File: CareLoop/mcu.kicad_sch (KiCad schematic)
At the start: 19 parts, among them J1_DEBUG1 Conn_01x04_Pin, SW1 SW_Push, U6 nRF52840, Y1 32Mhz

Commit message: updated version
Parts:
- removed AE1: Antenna_Chip, RF_Antenna:Johanson_2450AT18x100, symbol Device:Antenna_Chip
- removed C5: C, symbol Device:C_Small
- added C12: 4.7uF, Capacitor_SMD:C_0603_1608Metric_Pad1.08x0.95mm_HandSolder, symbol Device:C_Small
- added C18: 1.2pF, Capacitor_SMD:C_0603_1608Metric_Pad1.08x0.95mm_HandSolder, symbol Device:C_Small
- added C19: 1pF, Capacitor_SMD:C_0603_1608Metric_Pad1.08x0.95mm_HandSolder, symbol Device:C_Small
- added C27, C28: 14p, Capacitor_SMD:C_0603_1608Metric_Pad1.08x0.95mm_HandSolder, symbol Device:C_Small
- added C5: 1uF, Capacitor_SMD:C_0603_1608Metric_Pad1.08x0.95mm_HandSolder, symbol Device:C
- added L1: 2.2nH, Inductor_SMD:L_0603_1608Metric, symbol Device:L_Small
- added L2: 4.7nH, Inductor_SMD:L_0603_1608Metric, symbol Device:L_Small
- added Y2: 32.768kHz, Crystal:Crystal_SMD_0603-2Pin_6.0x3.5mm, symbol Device:Crystal
- C16: value C -> 820pF; footprint (none) -> Capacitor_SMD:C_0603_1608Metric_Pad1.08x0.95mm_HandSolder
- C17, C7: value C -> 1uF; footprint (none) -> Capacitor_SMD:C_0603_1608Metric_Pad1.08x0.95mm_HandSolder
- C4: value C -> 100nF; footprint (none) -> Capacitor_SMD:C_0603_1608Metric_Pad1.08x0.95mm_HandSolder
- C6: value C -> 100pF; footprint (none) -> Capacitor_SMD:C_0603_1608Metric_Pad1.08x0.95mm_HandSolder
- Y1: value 32Mhz -> 32MHz
- renumbered SW1 to Reset_SW1
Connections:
- net GND: now also D3.1 (K), C12.2, C27.2, C28.2, C5.2
- net at C10.1, U6.A22 (VDD), U6.AD14 (VDD)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: now also C5.1
- net at U6.AC5 (DECUSB): now also C12.1
- net Dminus: now reaches U6.AD4 (D-)
- net Dplus: now reaches U6.AD6 (D+)
- net INT_MAX: now reaches U6.AD8 (P0.13)
- net at U6.D2 (XL1/P0.00): now also C27.1, Y2.2
- net at U6.F2 (XL2/P0.01): now also C28.1, Y2.1
- net VSS_PA: now reaches U6.F23 (VSS_PA)
- net VSS_PA: now also C18.2, C19.2
- net at U6.H23 (ANT): now also C19.1, L2.2
- new net: C18.1, L1.2, L2.1
- new net ANT: L1.1
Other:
- moved on the sheet: C10, C8, C9, D3, J1_DEBUG1, R3, R4, R5, R7, Reset_SW1, U6, Y1

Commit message: WP: update Schematics
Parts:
- added C29: 4.7u, symbol Device:C_Small
- added L5: 10u, symbol Device:L_Small
- added L6: 15n, symbol Device:L_Small
- C17: value 1uF -> 1u; footprint Capacitor_SMD:C_0603_1608Metric_Pad1.08x0.95mm_HandSolder -> (none)
- C18: value 1.2pF -> 1.2p
- C19: value 1pF -> 1p
- C27, C28: value 14p -> 12p
- C5: value 1uF -> 4.7u
- C7: value 1uF -> 47n; footprint Capacitor_SMD:C_0603_1608Metric_Pad1.08x0.95mm_HandSolder -> (none)
- L1: value 2.2nH -> 2.2n
- L2: value 4.7nH -> 4.7n
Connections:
- net VSS_PA is gone; now on net GND: C18.2, C19.2, U6.F23 (VSS_PA)
- net GND: now also C17.2, C7.2, C29.2; no longer C17.1, C7.1
- net VCC: now also C10.1, C5.1, U6.A22 (VDD), U6.AD14 (VDD), U6.AD23 (VDD), U6.B1 (VDD), U6.W1 (VDD), U6.Y2 (VDDH)
- net at U6.E24 (DEC6): now also C17.1, C7.1, U6.B5 (DEC4), L6.2; no longer C17.2
- net VBUS: now reaches U6.AD2 (VBUS)
- net VBUS: now also C29.1
- net at U6.B3 (DCC): now also L5.1
- new net: L5.2, L6.1

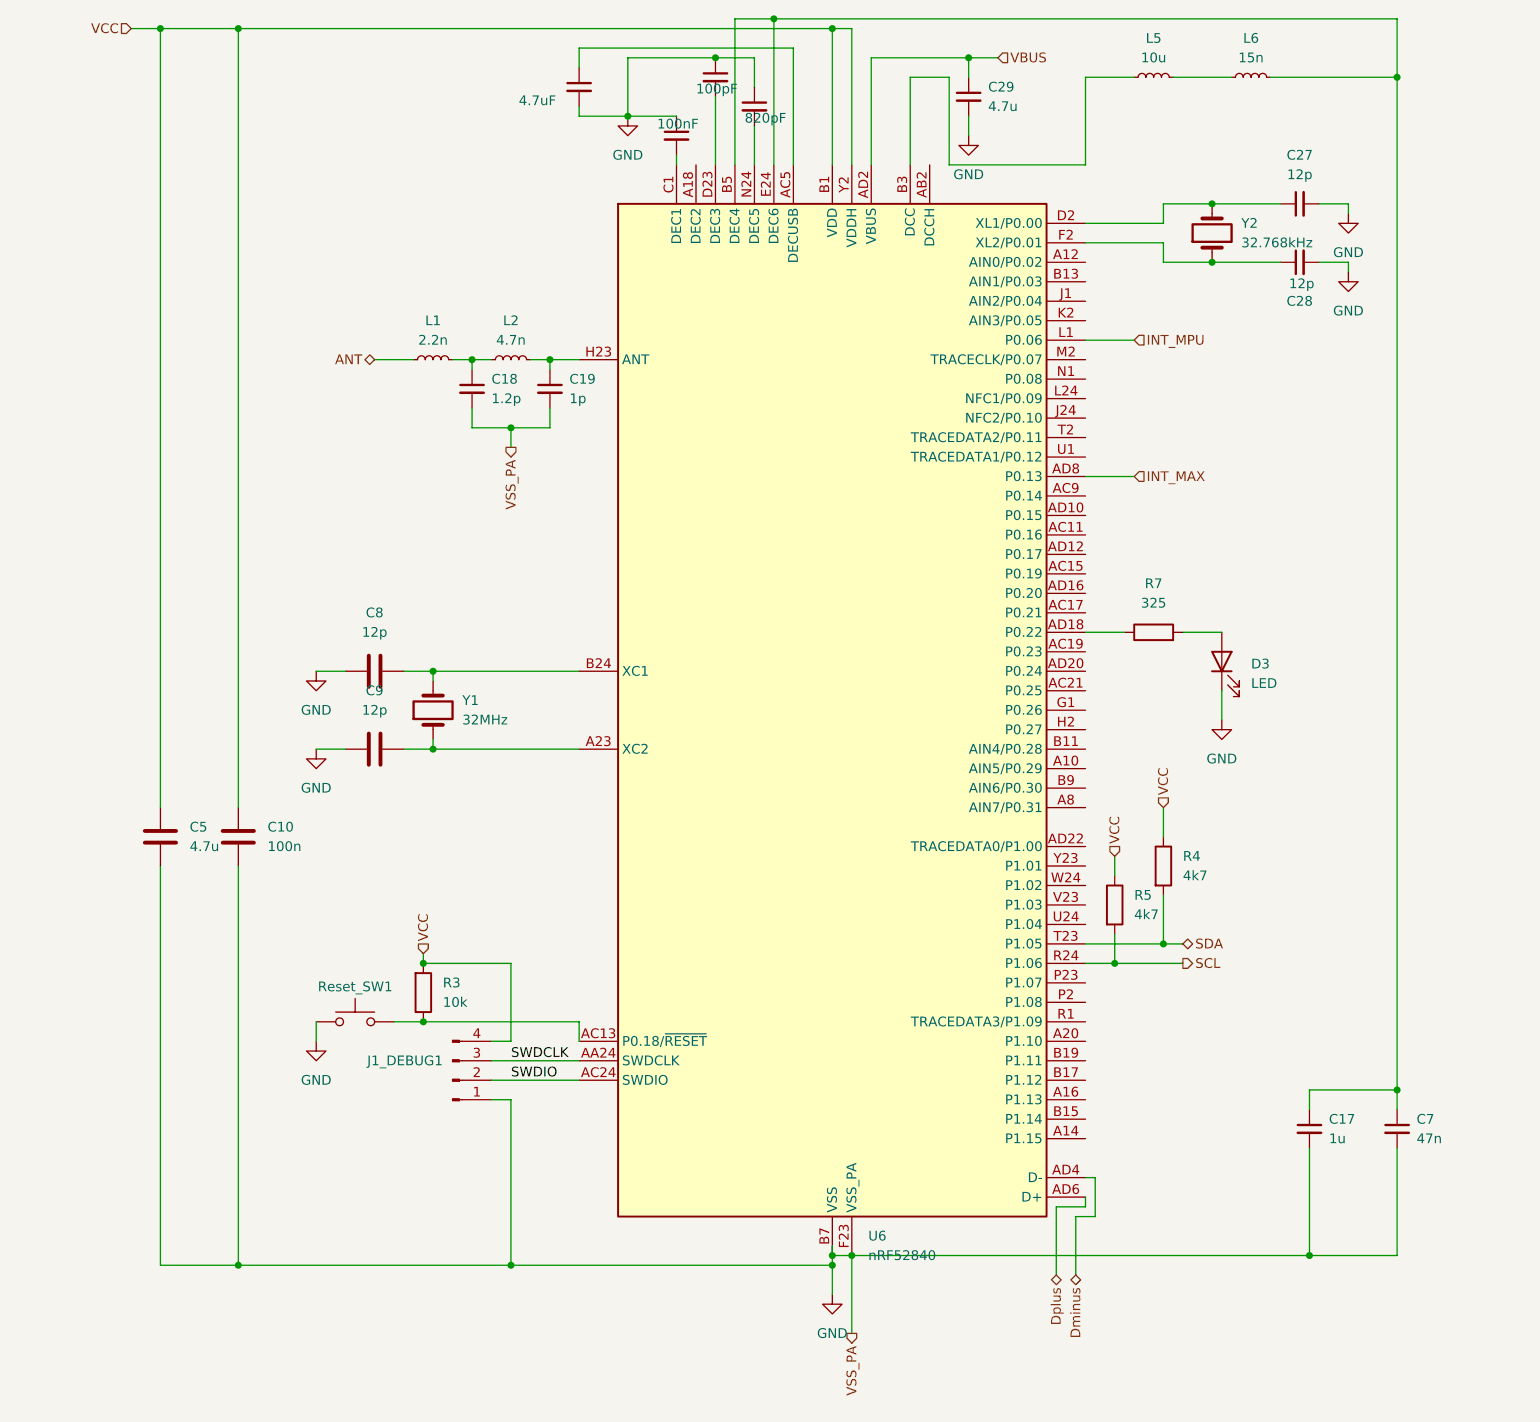
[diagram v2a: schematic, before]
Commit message: WP: Placement PCB Parts done
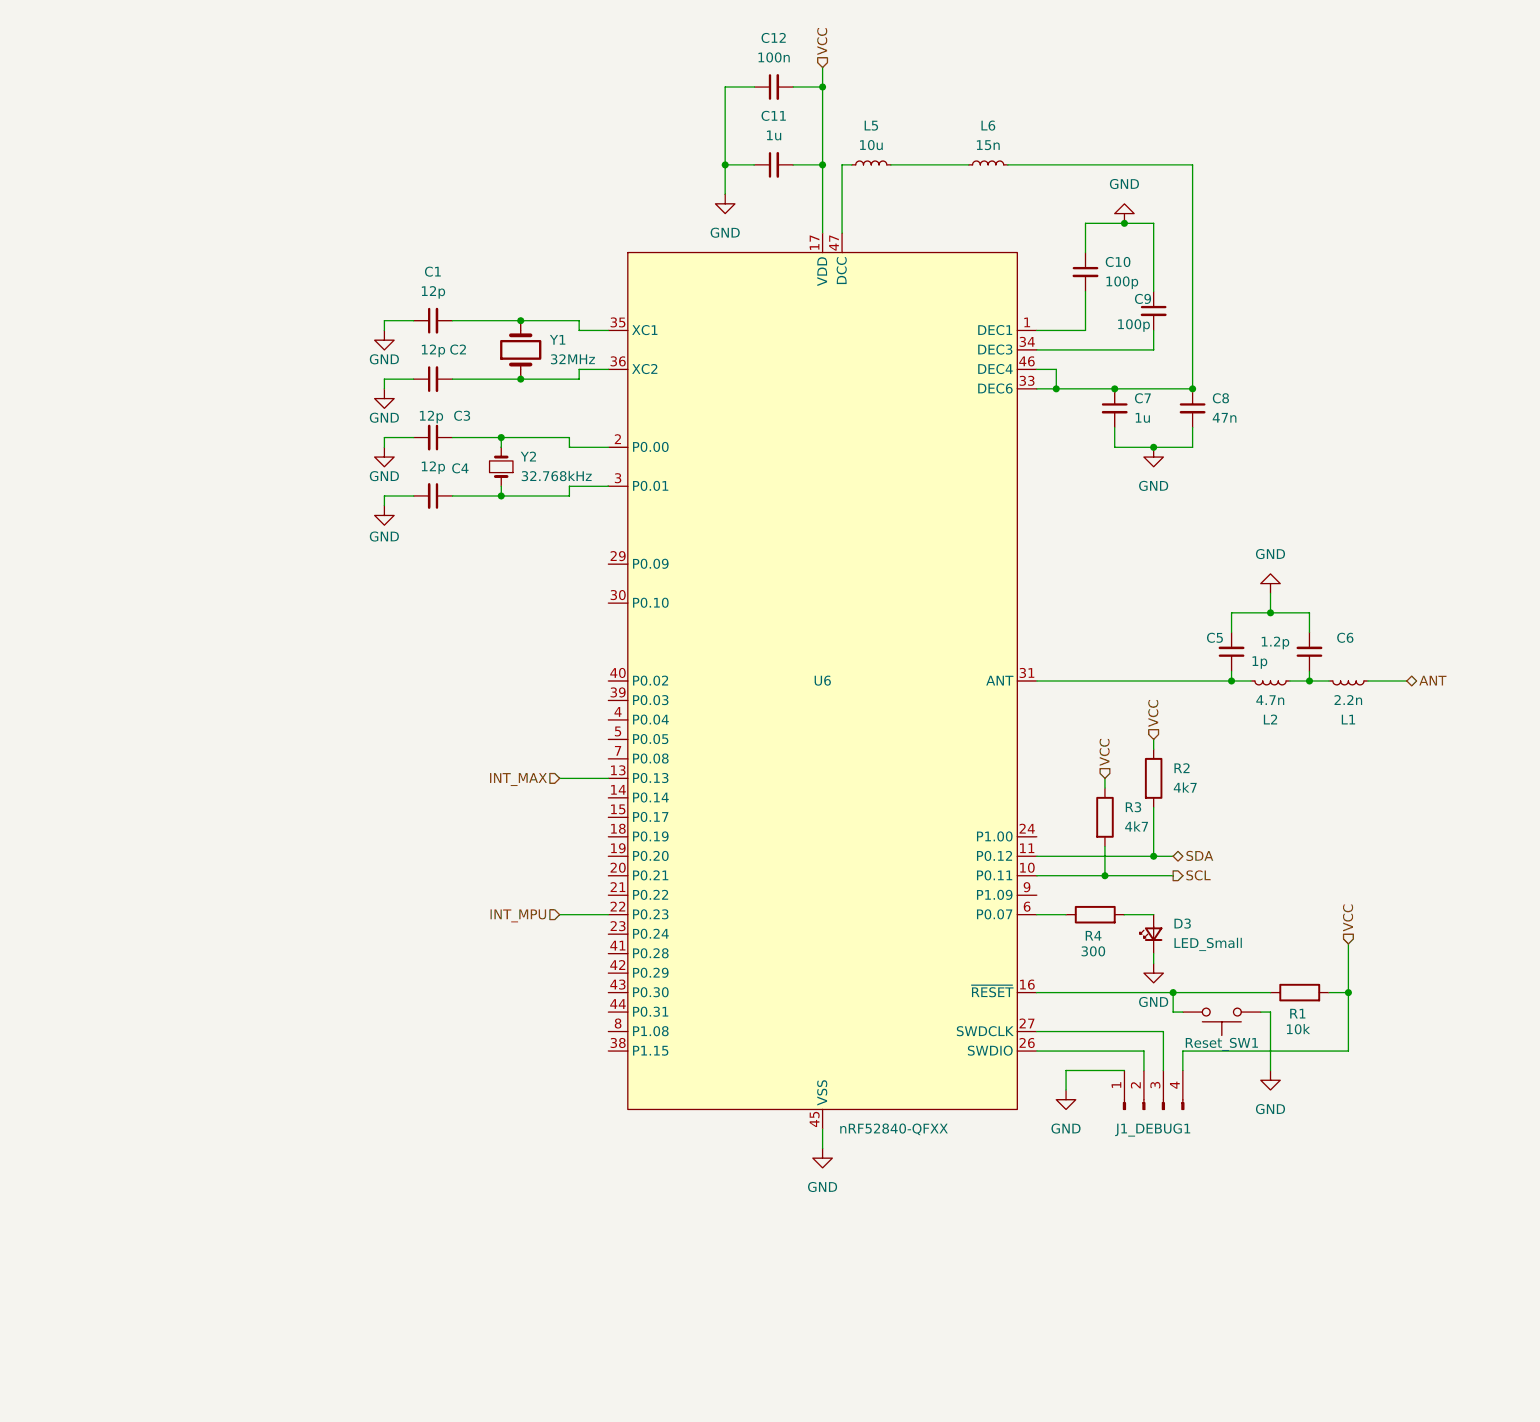
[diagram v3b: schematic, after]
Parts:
- removed C10: 100n, Capacitor_SMD:C_0603_1608Metric_Pad1.08x0.95mm_HandSolder, symbol Device:C
- removed C16: 820pF, Capacitor_SMD:C_0603_1608Metric_Pad1.08x0.95mm_HandSolder, symbol Device:C_Small
- removed C17: 1u, symbol Device:C_Small
- removed C29: 4.7u, symbol Device:C_Small
- removed C4: 100nF, Capacitor_SMD:C_0603_1608Metric_Pad1.08x0.95mm_HandSolder, symbol Device:C_Small
- removed C5: 4.7u, Capacitor_SMD:C_0603_1608Metric_Pad1.08x0.95mm_HandSolder, symbol Device:C
- removed C6: 100pF, Capacitor_SMD:C_0603_1608Metric_Pad1.08x0.95mm_HandSolder, symbol Device:C_Small
- removed C8, C9: 12p, Capacitor_SMD:C_0603_1608Metric_Pad1.08x0.95mm_HandSolder, symbol Device:C
- removed D3: LED, LED_SMD:LED_1206_3216Metric_Pad1.42x1.75mm_HandSolder, symbol Device:LED
- removed R3: 10k, Resistor_SMD:R_0603_1608Metric_Pad0.98x0.95mm_HandSolder, symbol Device:R
- removed U6: nRF52840, Package_DFN_QFN:Nordic_AQFN-73-1EP_7x7mm_P0.5mm, symbol MCU_Nordic:nRF52840
- removed Y2: 32.768kHz, Crystal:Crystal_SMD_0603-2Pin_6.0x3.5mm, symbol Device:Crystal
- added C1, C2: 12p, Capacitor_SMD:C_0201_0603Metric_Pad0.64x0.40mm_HandSolder, symbol Device:C_Small
- added C10, C9: 100p, Capacitor_SMD:C_0201_0603Metric_Pad0.64x0.40mm_HandSolder, symbol Device:C_Small
- added C11: 1u, Capacitor_SMD:C_0402_1005Metric_Pad0.74x0.62mm_HandSolder, symbol Device:C_Small
- added C8: 47n, Capacitor_SMD:C_0201_0603Metric_Pad0.64x0.40mm_HandSolder, symbol Device:C_Small
- added D3: LED_Small, LED_SMD:LED_0402_1005Metric_Pad0.77x0.64mm_HandSolder, symbol Device:LED_Small
- added R1: 10k, Resistor_SMD:R_0402_1005Metric_Pad0.72x0.64mm_HandSolder, symbol Device:R
- added U6: nRF52840-QFXX, Package_DFN_QFN:QFN-48-1EP_6x6mm_P0.4mm_EP4.6x4.6mm_ThermalVias, symbol PCM_nordic-lib-kicad-nrf52:nRF52840-QFXX
- added Y2: 32.768kHz, Crystal:Crystal_SMD_MicroCrystal_CM9V-T1A-2Pin_1.6x1.0mm_HandSoldering, symbol Device:Crystal_Small
- C12: value 4.7uF -> 100n; footprint Capacitor_SMD:C_0603_1608Metric_Pad1.08x0.95mm_HandSolder -> Capacitor_SMD:C_0201_0603Metric_Pad0.64x0.40mm_HandSolder
- C3: renamed from C28; footprint Capacitor_SMD:C_0603_1608Metric_Pad1.08x0.95mm_HandSolder -> Capacitor_SMD:C_0201_0603Metric_Pad0.64x0.40mm_HandSolder
- C4: renamed from C27; footprint Capacitor_SMD:C_0603_1608Metric_Pad1.08x0.95mm_HandSolder -> Capacitor_SMD:C_0201_0603Metric_Pad0.64x0.40mm_HandSolder
- C5: renamed from C19; footprint Capacitor_SMD:C_0603_1608Metric_Pad1.08x0.95mm_HandSolder -> Capacitor_SMD:C_0201_0603Metric_Pad0.64x0.40mm_HandSolder
- C6: renamed from C18; footprint Capacitor_SMD:C_0603_1608Metric_Pad1.08x0.95mm_HandSolder -> Capacitor_SMD:C_0201_0603Metric_Pad0.64x0.40mm_HandSolder
- C7: value 47n -> 1u; footprint (none) -> Capacitor_SMD:C_0402_1005Metric_Pad0.74x0.62mm_HandSolder
- L1, L2: footprint Inductor_SMD:L_0603_1608Metric -> Inductor_SMD:L_0402_1005Metric_Pad0.77x0.64mm_HandSolder
- L5: footprint (none) -> Inductor_SMD:L_0603_1608Metric_Pad1.05x0.95mm_HandSolder
- L6: footprint (none) -> Inductor_SMD:L_0201_0603Metric_Pad0.64x0.40mm_HandSolder
- R2: renamed from R4; footprint Resistor_SMD:R_0603_1608Metric_Pad0.98x0.95mm_HandSolder -> Resistor_SMD:R_0402_1005Metric_Pad0.72x0.64mm_HandSolder
- R3: renamed from R5; footprint Resistor_SMD:R_0603_1608Metric_Pad0.98x0.95mm_HandSolder -> Resistor_SMD:R_0402_1005Metric_Pad0.72x0.64mm_HandSolder
- R4: renamed from R7; value 325 -> 300; footprint Resistor_SMD:R_0603_1608Metric_Pad0.98x0.95mm_HandSolder -> Resistor_SMD:R_0402_1005Metric_Pad0.72x0.64mm_HandSolder
- Y1: footprint Crystal:Crystal_SMD_0603-2Pin_6.0x3.5mm -> Oscillator:Oscillator_SMD_Abracon_ASCO-4Pin_1.6x1.2mm
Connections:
- net GND: now also C12.1, C1.1, C10.1, C11.1, C2.1, C8.2, C9.1, D3.1 (K), U6.32 (VSS_PA), U6.45 (VSS), U6.49 (VSS); no longer C12.2
- net INT_MAX: now also U6.13 (P0.13)
- net INT_MPU: now also U6.22 (P0.23)
- net SCL: now also U6.10 (P0.11)
- net SDA: now also U6.11 (P0.12)
- net VCC: now also C12.2, C11.2, R1.2, U6.12 (VDD), U6.17 (VDD), U6.25 (VDD), U6.37 (VDD), U6.48 (VDD)
- net at R4.1: now also U6.6 (P0.07)
- net at R4.2: now also D3.2 (A)
- net at C7.1, L6.2: now also C8.1, U6.33 (DEC6), U6.46 (DEC4)
- net at C4.1: now also U6.3 (P0.01), Y2.1
- net at Y1.1: now also C2.2, U6.36 (XC2)
- net at Reset_SW1.1: now also R1.1, U6.16 (~{RESET})
- net at C3.1: now also U6.2 (P0.00), Y2.2
- net at C5.1, L2.2: now also U6.31 (ANT)
- net at L5.1: now also U6.47 (DCC)
- net SWDCLK: no longer names the net of J1_DEBUG1.3 (Pin_3)
- net SWDCLK: now also U6.27 (SWDCLK)
- net SWDIO: no longer names the net of J1_DEBUG1.2 (Pin_2)
- net SWDIO: now also U6.26 (SWDIO)
- new net: C10.2, U6.1 (DEC1)
- new net: C9.2, U6.34 (DEC3)
- new net: C1.2, U6.35 (XC1), Y1.3
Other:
- moved on the sheet: C3, C4, C5, C6, J1_DEBUG1, L1, L2, R2, R3, R4, Reset_SW1, Y1

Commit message: WP: updatet version with routing
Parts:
- U6: footprint Package_DFN_QFN:QFN-48-1EP_6x6mm_P0.4mm_EP4.6x4.6mm_ThermalVias -> Package_DFN_QFN:QFN-48-1EP_6x6mm_P0.4mm_EP4.6x4.6mm
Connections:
- net INT_MPU: now also U6.4 (P0.04); no longer U6.22 (P0.23)
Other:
- moved on the sheet: C1, C10, C11, C12, C2, C3, C4, C5, C6, C7, C8, C9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

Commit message: update routing
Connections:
- net INT_MAX: now also U6.22 (P0.23); no longer U6.13 (P0.13)
- net Status_LED: now reaches U6.19 (P0.20)
- net Status_LED: now also R4.1
- net at U6.6 (P0.07): no longer R4.1
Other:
- moved on the sheet: D3, R4
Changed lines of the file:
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@@
+	(wire
+		(pts
+			(xy 49.53 127) (xy 68.58 127)
+		)
+		(stroke
+			(width 0)
+			(type default)
+		)
+	)
 	(wire
 		(pts
@@
 	(wire
 		(pts
-			(xy 139.7 134.62) (xy 135.89 134.62)
-		)
-		(stroke
-			(width 0)
-			(type default)
-		)
-	)
-	(wire
-		(pts
 			(xy 39.37 66.04) (xy 39.37 64.77)
 		)
@@
 	(wire
 		(pts
+			(xy 36.83 127) (xy 41.91 127)
+		)
+		(stroke
+			(width 0)
+			(type default)
+		)
+	)
+	(wire
+		(pts
 			(xy 48.26 80.01) (xy 54.61 80.01)
 		)
@@
 	(wire
 		(pts
-			(xy 124.46 134.62) (xy 128.27 134.62)
-		)
-		(stroke
-			(width 0)
-			(type default)
-		)
-	)
-	(wire
-		(pts
 			(xy 124.46 63.5) (xy 127 63.5)
 		)
@@
 	(wire
 		(pts
+			(xy 62.23 134.62) (xy 68.58 134.62)
+		)
+		(stroke
+			(width 0)
+			(type default)
+		)
+	)
+	(wire
+		(pts
 			(xy 64.77 57.15) (xy 64.77 58.42)
 		)
@@
 	(wire
 		(pts
-			(xy 139.7 139.7) (xy 139.7 140.97)
-		)
-		(stroke
-			(width 0)
-			(type default)
-		)
-	)
-	(wire
-		(pts
 			(xy 96.52 162.56) (xy 96.52 165.1)
 		)
@@
 	(wire
 		(pts
-			(xy 68.58 116.84) (xy 62.23 116.84)
-		)
-		(stroke
-			(width 0)
-			(type default)
-		)
-	)
-	(wire
-		(pts
 			(xy 96.52 36.83) (xy 96.52 45.72)
 		)
@@
 	(wire
 		(pts
+			(xy 36.83 132.08) (xy 36.83 133.35)
+		)
+		(stroke
+			(width 0)
+			(type default)
+		)
+	)
+	(wire
+		(pts
 			(xy 160.02 102.87) (xy 160.02 104.14)
 		)
@@
 			(width 0)
 			(type default)
+		)
+	)
+	(label "Status_LED"
+		(at 52.07 127 0)
+		(effects
+			(font
+				(size 1.27 1.27)
+			)
+			(justify left bottom)
 		)
 	)
 	(hierarchical_label "INT_MAX"
 		(shape input)
-		(at 62.23 116.84 180)
+		(at 62.23 134.62 180)
 		(effects
 			(font
@@
 	(symbol
 		(lib_id "Device:R")
-		(at 132.08 134.62 90)
+		(at 45.72 127 270)
 		(unit 1)
 		(exclude_from_sim no)
@@
 		(dnp no)
 		(property "Reference" "R4"
-			(at 131.826 137.414 90)
+			(at 45.974 124.206 90)
 			(effects
 				(font
@@
 		)
 		(property "Value" "300"
-			(at 131.826 139.446 90)
+			(at 45.974 122.174 90)
 			(effects
 				(font
@@
 		)
 		(property "Footprint" "Resistor_SMD:R_0402_1005Metric_Pad0.72x0.64mm_HandSolder"
-			(at 132.08 136.398 90)
+			(at 45.72 125.222 90)
 			(effects
 				(font
@@
 		)
 		(property "Datasheet" "~"
-			(at 132.08 134.62 0)
+			(at 45.72 127 0)
 			(effects
 				(font
@@
 		)
 		(property "Description" "Resistor"
-			(at 132.08 134.62 0)
+			(at 45.72 127 0)
 			(effects
 				(font
@@
 	(symbol
 		(lib_id "power:GND")
-		(at 139.7 140.97 0)
+		(at 36.83 133.35 0)
 		(unit 1)
 		(exclude_from_sim no)
@@
 		(fields_autoplaced yes)
 		(property "Reference" "#PWR025"
-			(at 139.7 147.32 0)
+			(at 36.83 139.7 0)
 			(effects
 				(font
@@
 		)
 		(property "Value" "GND"
-			(at 139.7 146.05 0)
+			(at 36.83 138.43 0)
 			(effects
 				(font
@@
 		)
 		(property "Footprint" ""
-			(at 139.7 140.97 0)
+			(at 36.83 133.35 0)
 			(effects
 				(font
@@
 		)
 		(property "Datasheet" ""
-			(at 139.7 140.97 0)
+			(at 36.83 133.35 0)
 			(effects
 				(font
@@
 		)
 		(property "Description" "Power symbol creates a global label with name \"GND\" , ground"
-			(at 139.7 140.97 0)
+			(at 36.83 133.35 0)
 			(effects
 				(font
@@
 	(symbol
 		(lib_id "Device:LED_Small")
-		(at 139.7 137.16 90)
+		(at 36.83 129.54 90)
 		(unit 1)
 		(exclude_from_sim no)
@@
 		(fields_autoplaced yes)
 		(property "Reference" "D3"
-			(at 142.24 135.8264 90)
+			(at 39.37 128.2064 90)
 			(effects
 				(font
@@
 		)
 		(property "Value" "LED_Small"
-			(at 142.24 138.3664 90)
+			(at 39.37 130.7464 90)
 			(effects
 				(font
@@
 		)
 		(property "Footprint" "LED_SMD:LED_0402_1005Metric_Pad0.77x0.64mm_HandSolder"
-			(at 139.7 137.16 90)
+			(at 36.83 129.54 90)
 			(effects
 				(font
@@
 		)
 		(property "Datasheet" "~"
-			(at 139.7 137.16 90)
+			(at 36.83 129.54 90)
 			(effects
 				(font
@@
 		)
 		(property "Description" "Light emitting diode, small symbol"
-			(at 139.7 137.16 0)
+			(at 36.83 129.54 0)
 			(effects
 				(font
@@
 		)
 		(property "Sim.Pin" "1=K 2=A"
-			(at 139.7 137.16 0)
-			(effects
-				(font
+			(at 36.83 129.54 0)
+			(effects
+				(font
